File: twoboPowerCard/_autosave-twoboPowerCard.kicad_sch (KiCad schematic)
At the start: 14 parts, among them J4 Conn_01x04_Pin, Q1 IRF5305PbF, Q2 IRF5305PbF, U3 TSR2-2450, U4 TSR2-2433, U5 TSR2-2450

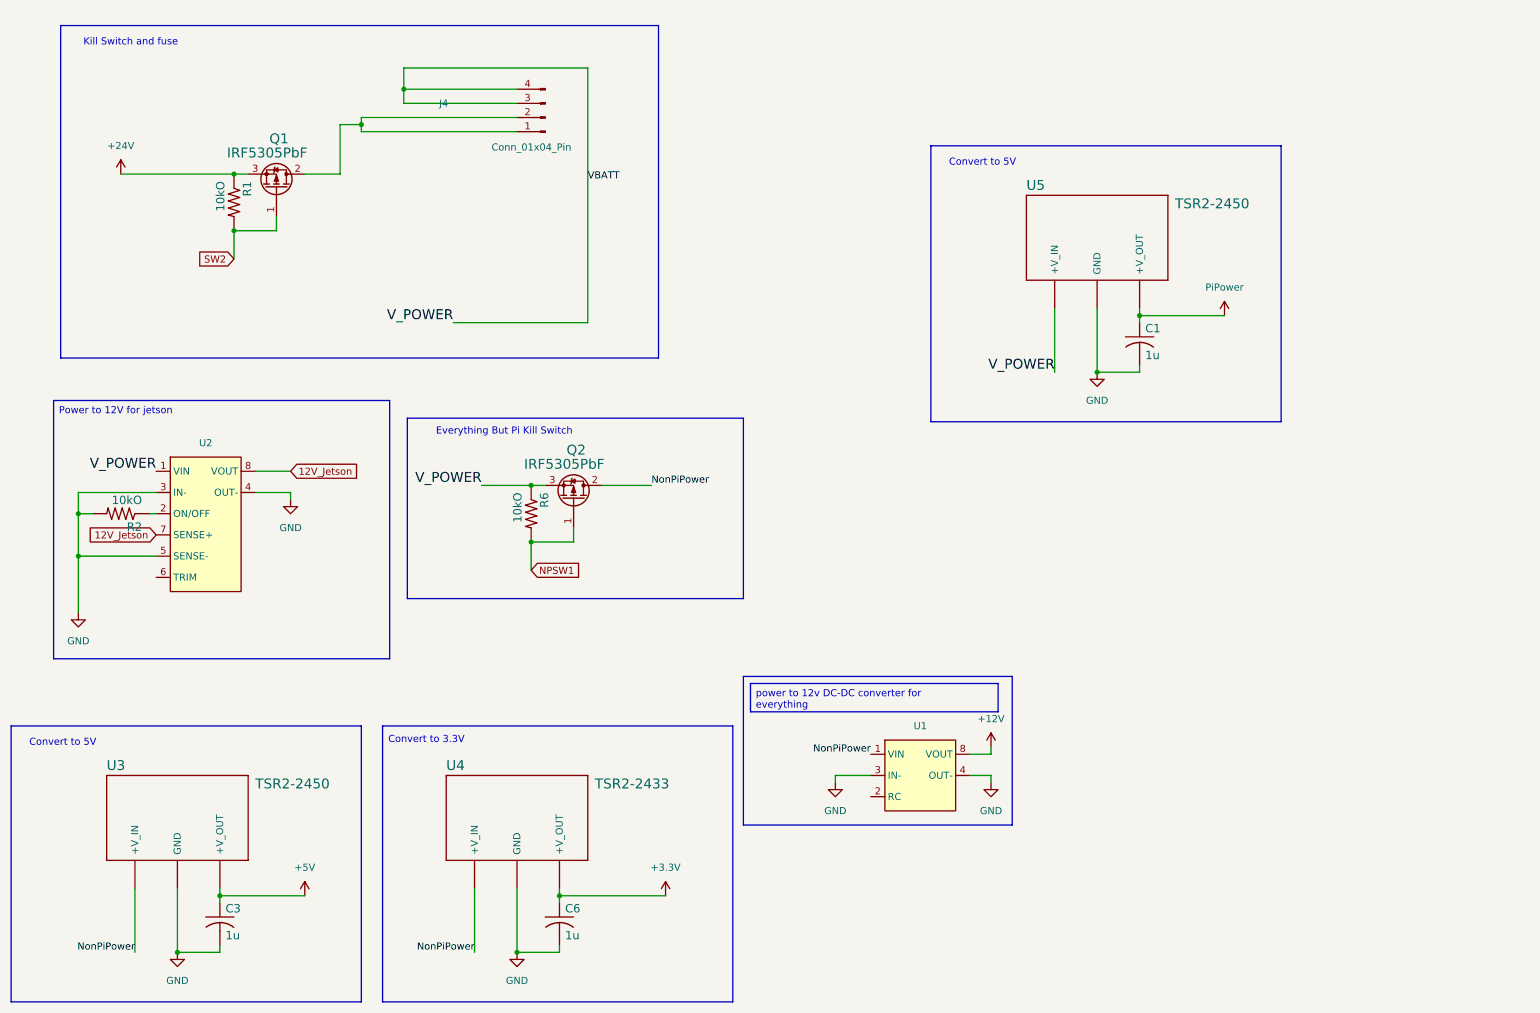
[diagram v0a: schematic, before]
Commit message: Added connector to power card
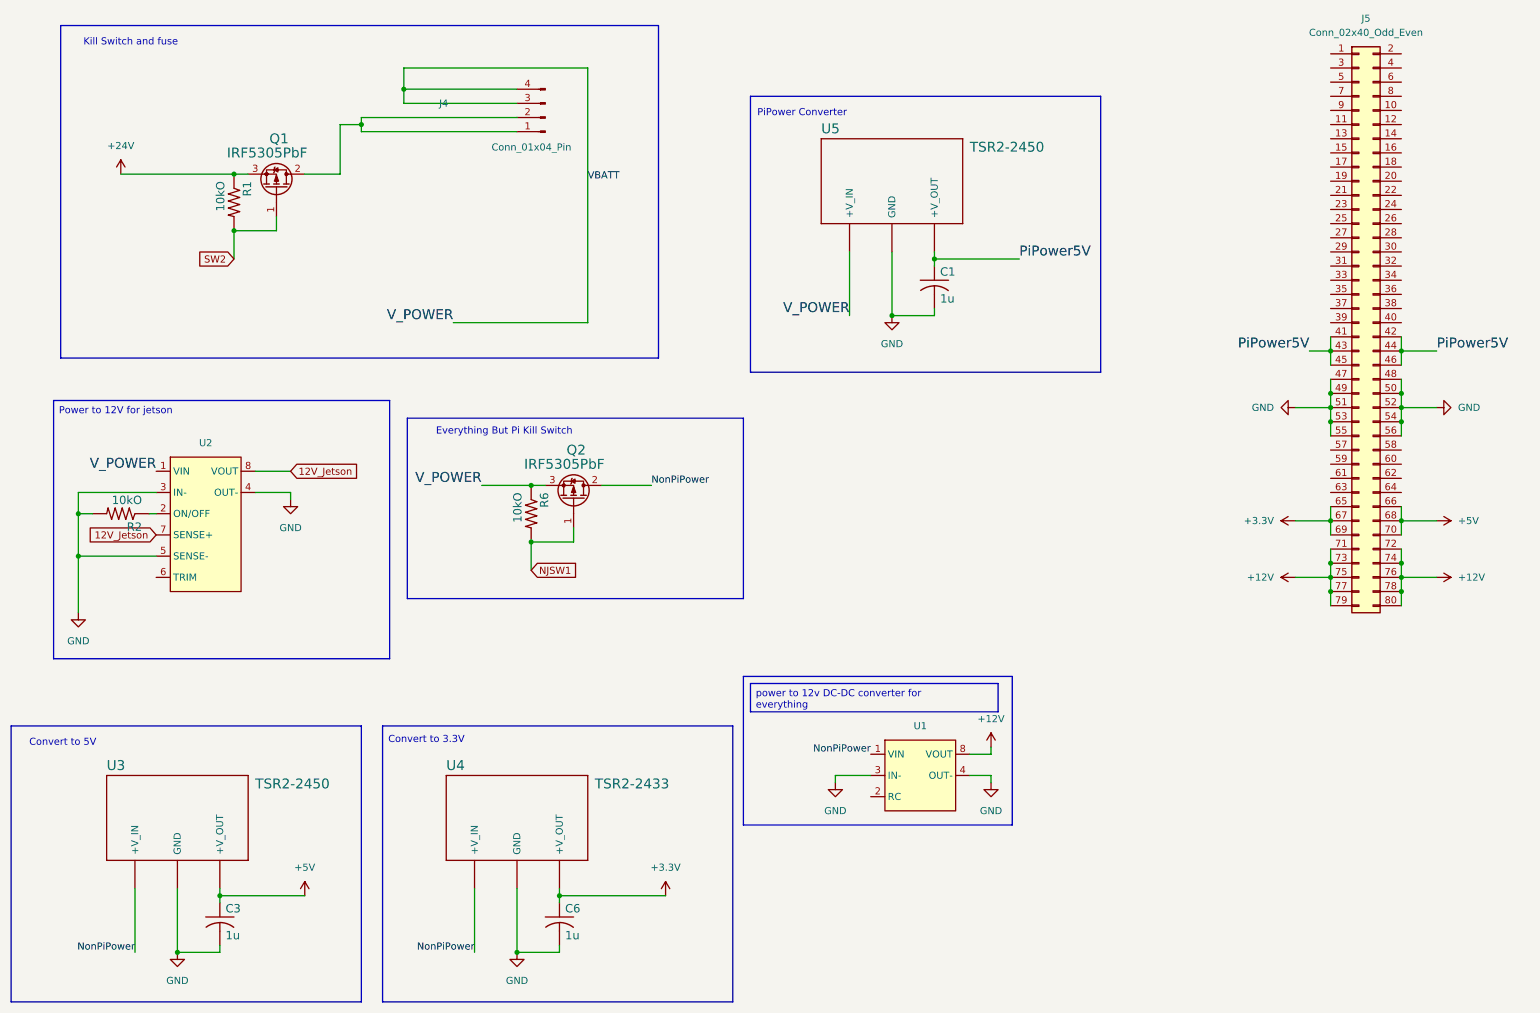
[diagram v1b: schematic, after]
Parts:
- added J5: Conn_02x40_Odd_Even, Samtec Custom:Samtec_HLE-140-02-L-DV-PE_2x40_P2.54mm_Horizontal, symbol Connector_Generic:Conn_02x40_Odd_Even
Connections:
- net +12V: now also J5.71 (Pin_71), J5.72 (Pin_72), J5.73 (Pin_73), J5.74 (Pin_74), J5.75 (Pin_75), J5.76 (Pin_76), J5.77 (Pin_77), J5.78 (Pin_78), J5.79 (Pin_79), J5.80 (Pin_80)
- net +3.3V: now also J5.65 (Pin_65), J5.67 (Pin_67), J5.69 (Pin_69)
- net +5V: now also J5.66 (Pin_66), J5.68 (Pin_68), J5.70 (Pin_70)
- net GND: now also J5.47 (Pin_47), J5.48 (Pin_48), J5.49 (Pin_49), J5.50 (Pin_50), J5.51 (Pin_51), J5.52 (Pin_52), J5.53 (Pin_53), J5.54 (Pin_54), J5.55 (Pin_55), J5.56 (Pin_56)
- net NPSW1 renamed NJSW1
- net PiPower renamed PiPower5V
- net PiPower5V: now also J5.41 (Pin_41), J5.42 (Pin_42), J5.43 (Pin_43), J5.44 (Pin_44), J5.45 (Pin_45), J5.46 (Pin_46)
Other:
- note added: "PiPower Converter"
